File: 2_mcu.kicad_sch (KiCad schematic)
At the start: 1 part

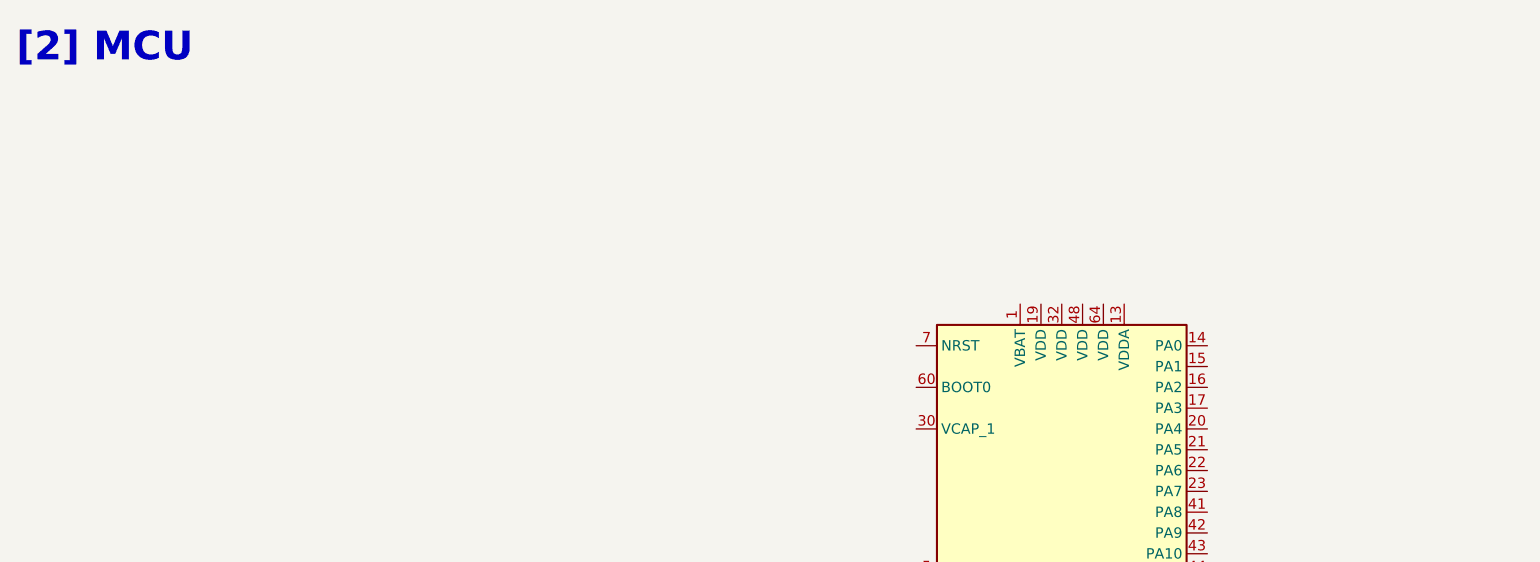
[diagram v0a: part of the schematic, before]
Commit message: feat/chore: MCU supply caps and filter circuitry and updated component references in power supply sheet
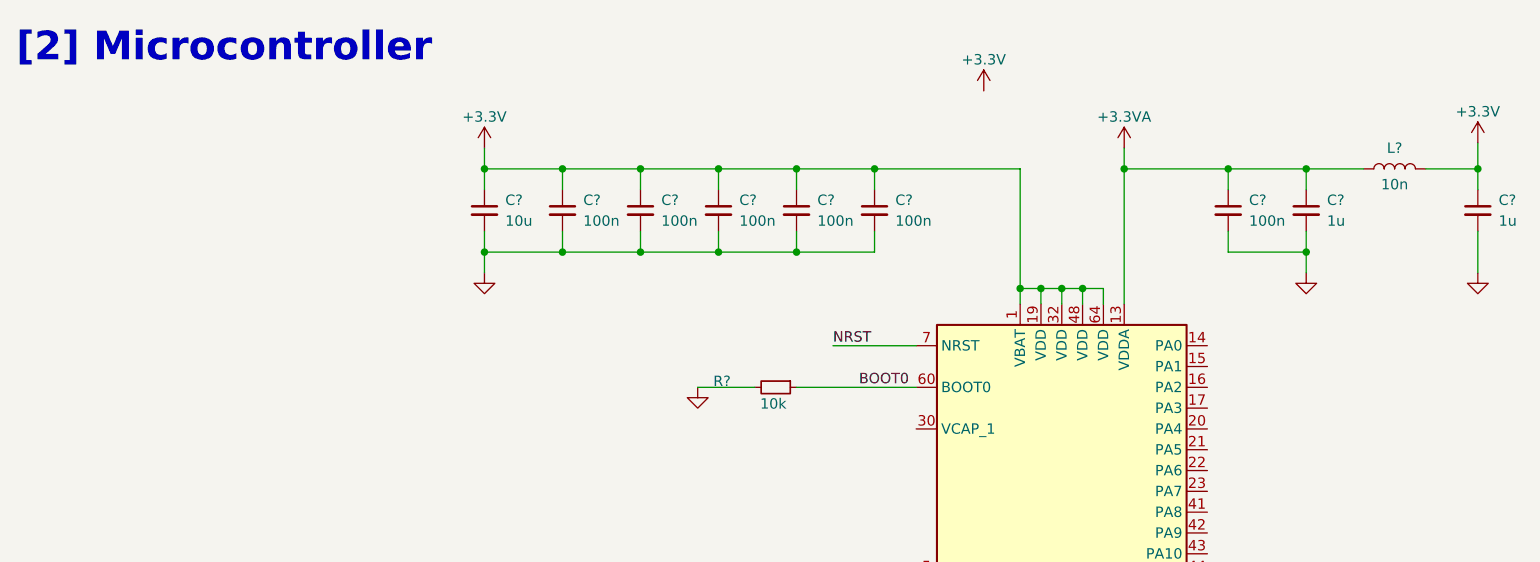
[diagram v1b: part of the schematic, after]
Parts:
- added C? (x2): 1u, symbol Device:C_Small
- added C? (x6): 100n, symbol Device:C_Small
- added C?: 10u, symbol Device:C_Small
- added L?: 10n, symbol Device:L
- added R?: 10k, symbol Device:R_Small
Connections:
- net GND: now also C?.2, C?.2, C?.2, C?.2, C?.2, C?.2, C?.2, C?.2, C?.2, R?.2
- net +3.3V: now reaches U?.1 (VBAT)
- net +3.3V: now also U?.19 (VDD), U?.32 (VDD), U?.48 (VDD), U?.64 (VDD), C?.1, C?.1, C?.1, C?.1, C?.1, C?.1, C?.1, L?.2
- net +3.3VA: now reaches U?.13 (VDDA)
- net +3.3VA: now also C?.1, C?.1, L?.1
- net BOOT0: now reaches U?.60 (BOOT0)
- net BOOT0: now also R?.1
- net NRST: now reaches U?.7 (NRST)
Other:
- note added: "[2] Microcontroller"
- note removed: "[2] MCU"

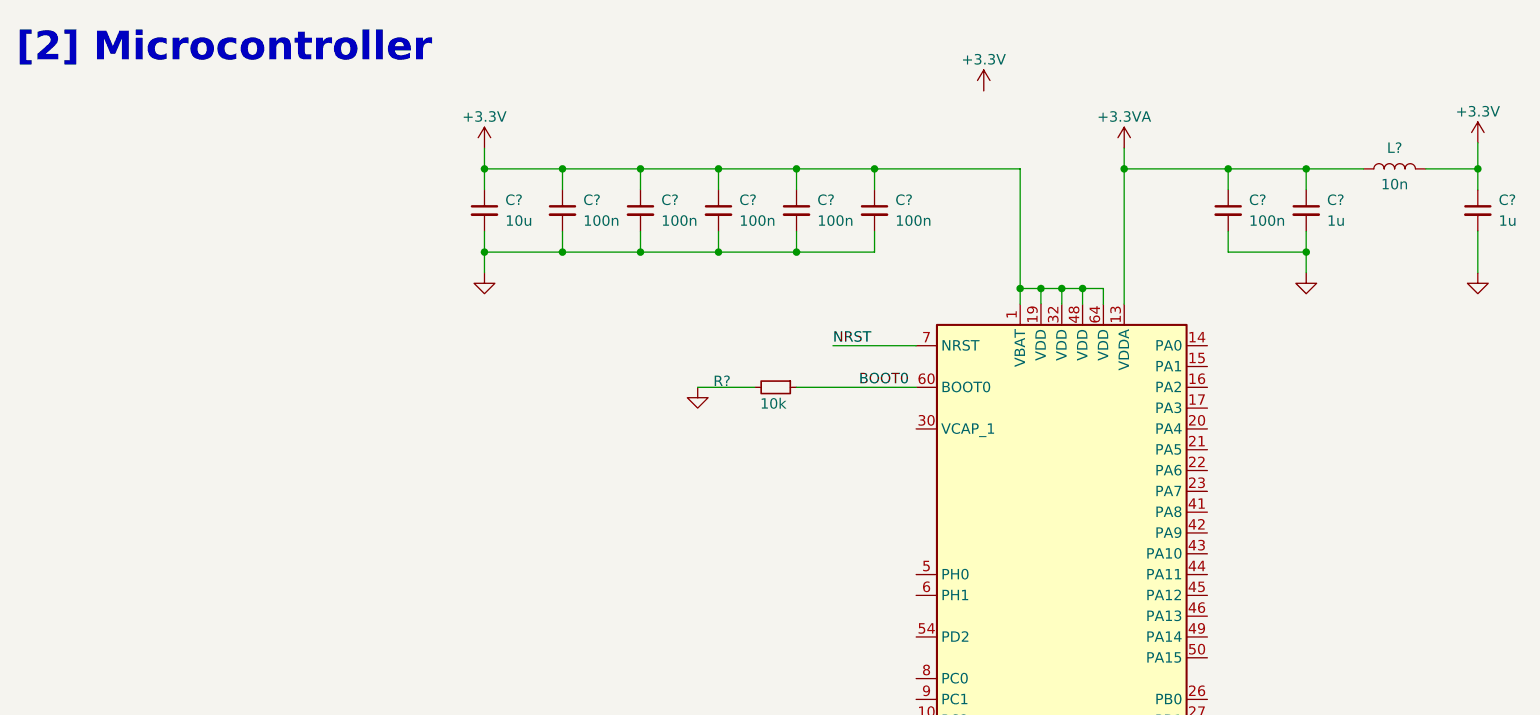
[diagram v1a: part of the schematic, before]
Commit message: feat: initial peripheral circuitry for MCU
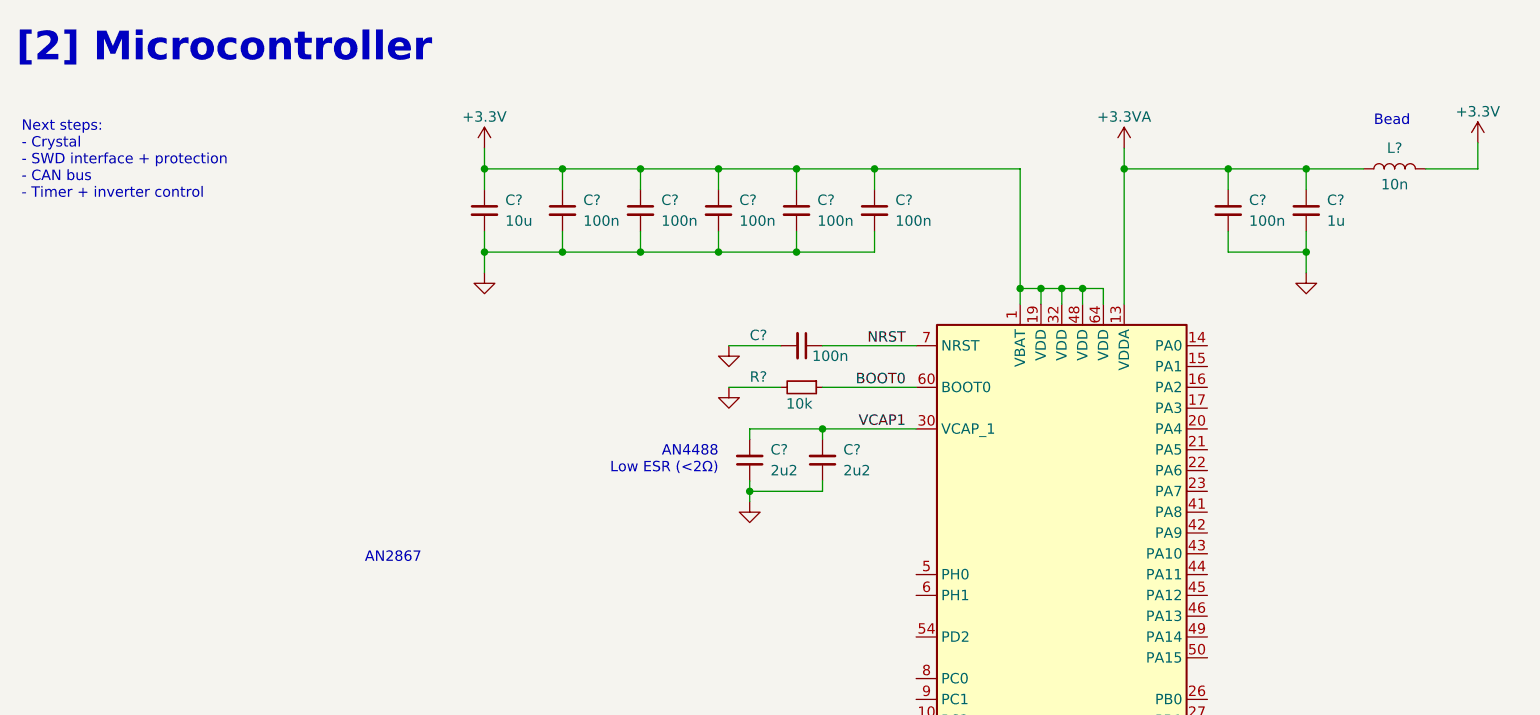
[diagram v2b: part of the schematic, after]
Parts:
- removed C?: 1u, symbol Device:C_Small
- added C? (x2): 2u2, symbol Device:C_Small
- added C?: 100n, symbol Device:C_Small
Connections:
- net GND: now also C?.1, C?.1, C?.2
- net NRST: now also C?.1
- net VCAP1: now reaches U?.30 (VCAP_1)
- net VCAP1: now also C?.2, C?.2
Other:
- note added: "AN2867"
- note added: "AN4488 Low ESR (<2Ω)"
- note added: "Bead"
- note added: "Next steps: - Crystal - SWD interface + protection - CAN bus - Timer + inverter control"
- moved on the sheet: R?

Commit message: feat: oscillator design
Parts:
- added C? (x2): 10p, symbol Device:C_Small
- added R?: 100, symbol Device:R_Small
- added Y?: 25MHz, symbol Device:Crystal_GND24
- L?: value 10n -> WE742792625
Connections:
- net GND: now also C?.2, C?.2, Y?.2, Y?.4
- net HSE_IN: now reaches U?.5 (PH0)
- net HSE_IN: now also C?.1, Y?.1
- net HSE_OUT: now reaches U?.6 (PH1)
- net HSE_OUT: now also R?.2
- new net XTAL_IN: C?.1, R?.1, Y?.3
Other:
- note added: "App Note: AN2867"
- note added: "C_{L}=10pF ESR=40R"
- note added: "Next steps: - SWD interface + protection - CAN bus - Timer + inverter control"
- note added: "Place reset button in parallel"
- note removed: "AN2867"
- note removed: "Next steps: - Crystal - SWD interface + protection - CAN bus - Timer + inverter control"

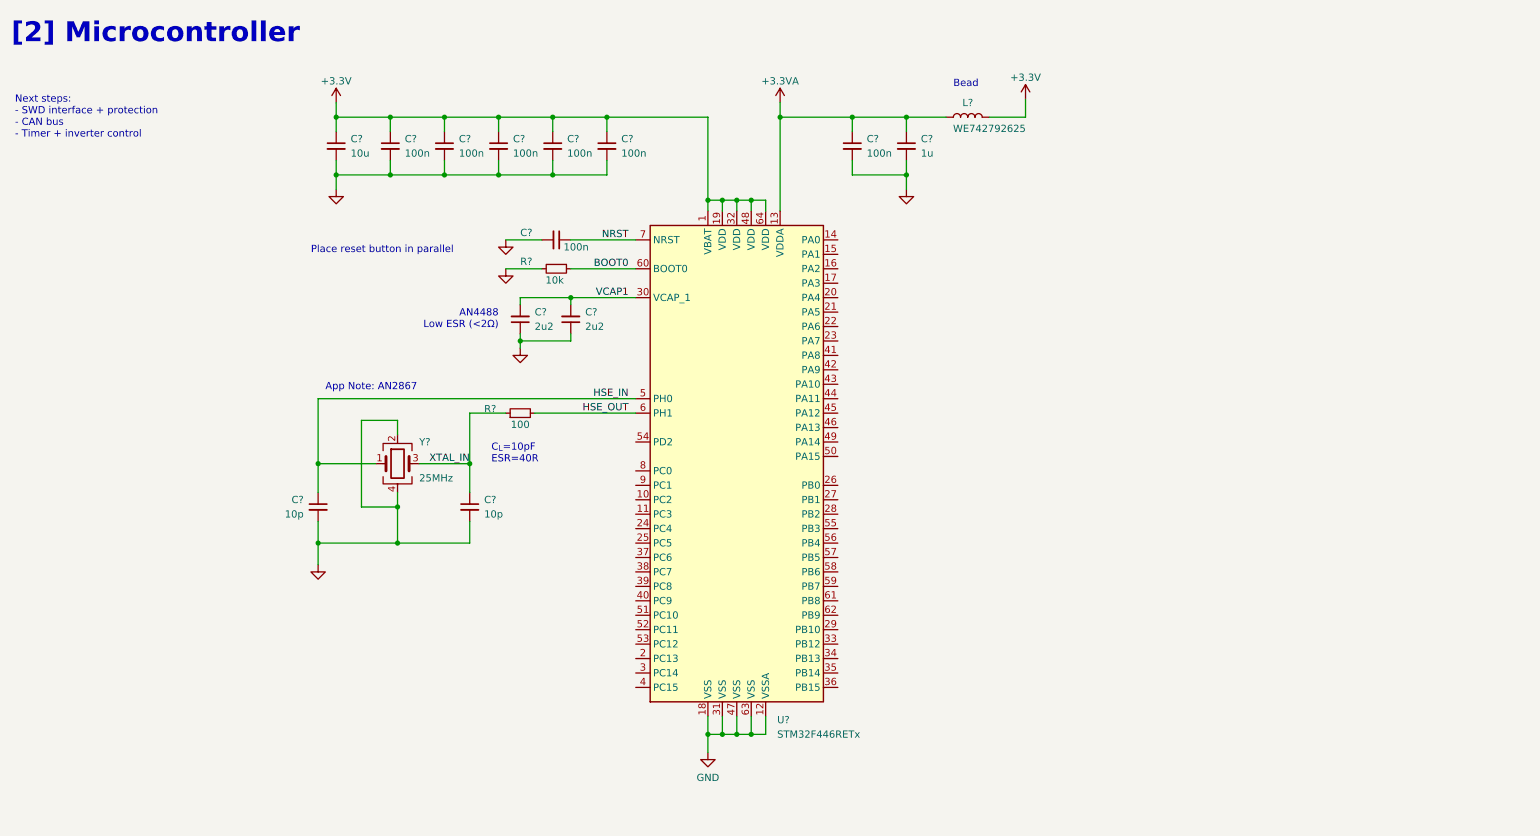
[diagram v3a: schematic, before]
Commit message: reset button and SWD tag connect
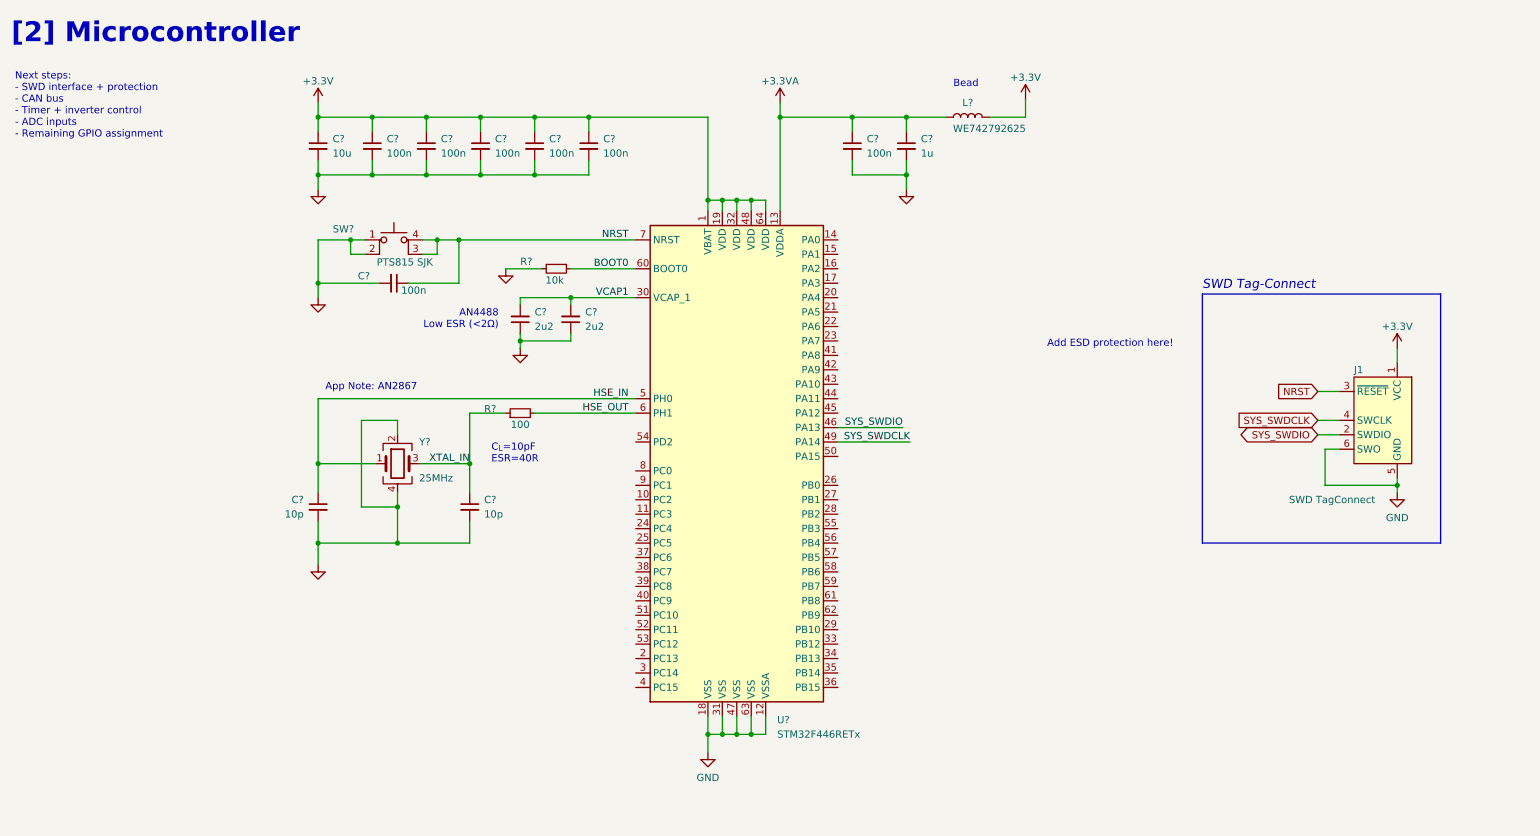
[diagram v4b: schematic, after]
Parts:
- added J1: SWD TagConnect, Connector:Tag-Connect_TC2030-IDC-FP_2x03_P1.27mm_Vertical, symbol Connector:Conn_ARM_SWD_TagConnect_TC2030
- added SW?: PTS815 SJK, symbol Switch:SW_MEC_5E
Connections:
- net +3.3V: now also J1.1 (VCC)
- net GND: now also J1.5 (GND), J1.6 (SWO), SW?.1, SW?.2
- net NRST: now also J1.3 (~{RESET}), SW?.3 (K), SW?.4 (A)
- net SYS_SWDIO: now reaches U?.46 (PA13)
- net SYS_SWDIO: now also J1.2 (SWDIO)
- net SYS_SWDCLK: now reaches U?.49 (PA14)
- net SYS_SWDCLK: now also J1.4 (SWCLK)
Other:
- note added: "Add ESD protection here!"
- note added: "Next steps: - SWD interface + protection - CAN bus - Timer + inverter control - ADC inputs - Remaining GPIO assignment"
- note added: "SWD Tag-Connect"
- note removed: "Next steps: - SWD interface + protection - CAN bus - Timer + inverter control"
- note removed: "Place reset button in parallel"
- moved on the sheet: C?

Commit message: swd protection
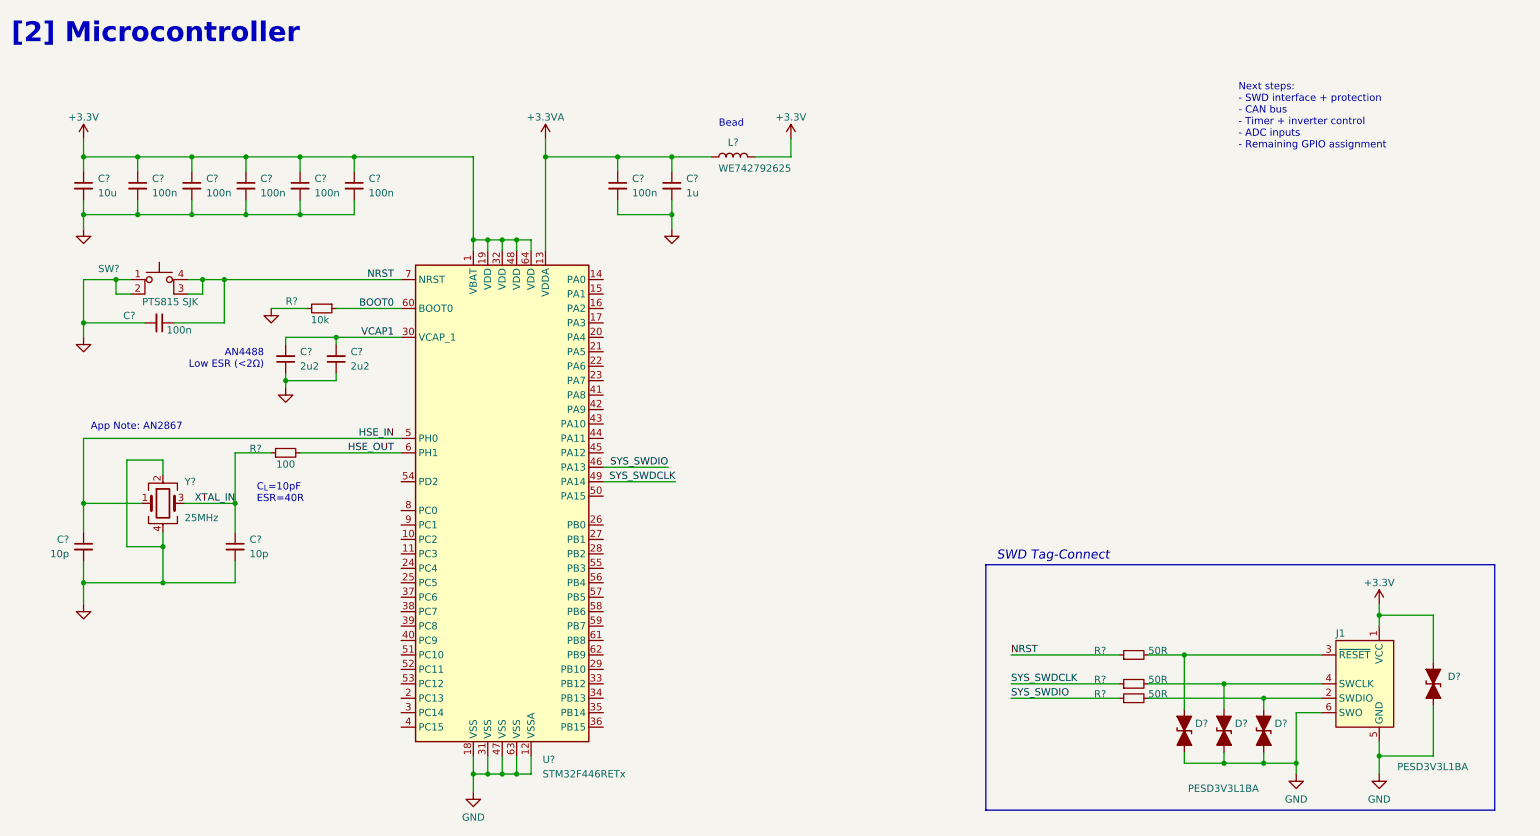
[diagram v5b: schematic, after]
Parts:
- added D? (x4): PESD3V3L1BA, Diode_SMD:D_SOD-323_HandSoldering, symbol Device:D_TVS_Filled
- added R? (x3): 50R, symbol Device:R_Small
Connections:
- net +3.3V: now also D?.2 (A2)
- net GND: now also D?.1 (A1), D?.1 (A1), D?.1 (A1), D?.1 (A1)
- net NRST: now also R?.1; no longer J1.3 (~{RESET})
- net SYS_SWDCLK: now also R?.1; no longer J1.4 (SWCLK)
- net SYS_SWDIO: now also R?.1; no longer J1.2 (SWDIO)
- new net: D?.2 (A2), J1.4 (SWCLK), R?.2
- new net: D?.2 (A2), J1.2 (SWDIO), R?.2
- new net: D?.2 (A2), J1.3 (~{RESET}), R?.2
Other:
- note removed: "Add ESD protection here!"
- moved on the sheet: C?, J1, L?, R?, SW?, U?, Y?
